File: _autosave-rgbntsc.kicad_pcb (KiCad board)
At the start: 2 copper layers, 50 x 70 mm, 40 parts, among them J1 USB_C_Receptacle_Power, J2 VGA, J3 SCART_CONN, J4 Mini-DIN-4, U1 LM1881, U102 74AHCT1G86, U103 74AHCT1G86, U2 SC6206B-65K5, U3 CXA2075, X1 ASE-14.32MHz

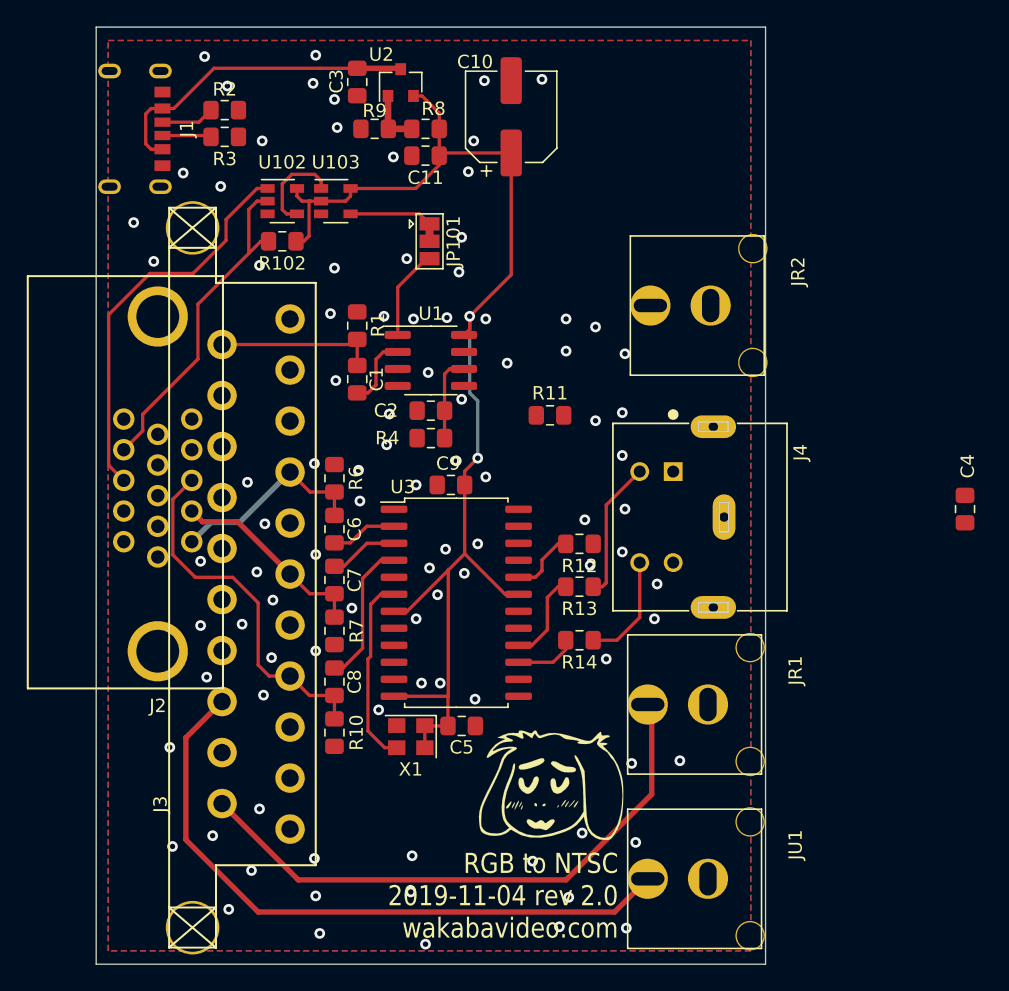
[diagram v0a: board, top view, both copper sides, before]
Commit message: CXA2075
Replaces AD724 with CXA2075, also adds GBS compatible RGB out header
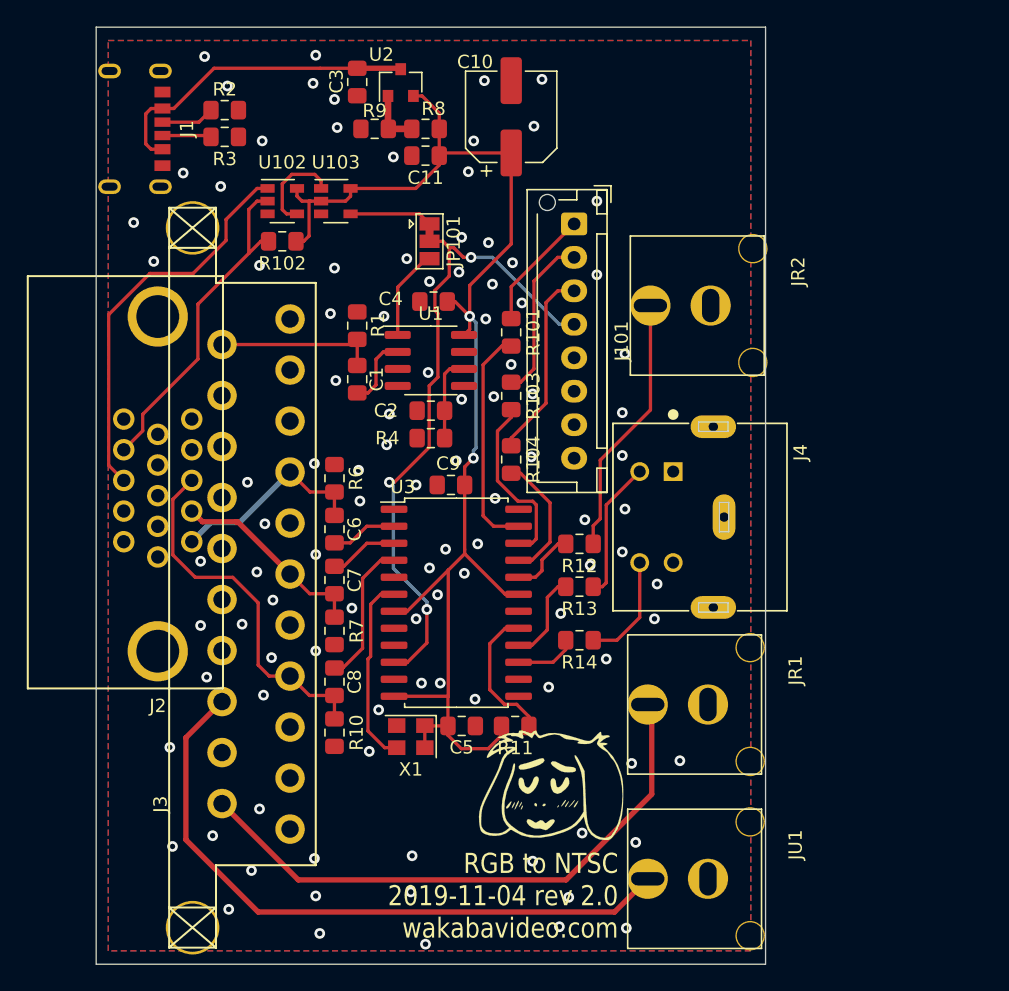
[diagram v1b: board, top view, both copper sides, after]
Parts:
- added J101: Conn_01x08, Connector_JST:JST_XH_B8B-XH-AM_1x08_P2.50mm_Vertical, F.Cu at (55.7, 54.7)
- added R101: 75, Resistor_SMD:R_0805_2012Metric_Pad1.15x1.40mm_HandSolder, F.Cu at (51.0, 62.8)
- added R103: 75, Resistor_SMD:R_0805_2012Metric_Pad1.15x1.40mm_HandSolder, F.Cu at (51.0, 67.5)
- added R104: 75, Resistor_SMD:R_0805_2012Metric_Pad1.15x1.40mm_HandSolder, F.Cu at (51.0, 72.3)
- moved C4 42.6 mm to (45.2, 60.5), turned to 180 degrees
- moved R11 23.3 mm to (51.3, 92.2), turned to 180 degrees
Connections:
- U3 pad 10: Net-(U3-Pad10) -> /SYNC
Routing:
- net /SYNC: track 0.00 -> 49.4 mm, vias 0 -> 3
- net Net-(JR2-Pad1): track 0.00 -> 19.6 mm
- net Net-(R101-Pad2): track 0.00 -> 16.9 mm
- net Net-(J101-Pad3): track 0.00 -> 14.2 mm
- net Net-(R103-Pad2): track 0.00 -> 13.4 mm
- net Net-(J101-Pad2): track 0.00 -> 12.4 mm
- net Net-(R11-Pad1): track 0.00 -> 10.5 mm
- net Net-(R104-Pad2): track 0.00 -> 9.67 mm
- net Net-(J101-Pad1): track 0.00 -> 9.02 mm
- net VCC: track 93.2 -> 101.5 mm
- net Net-(R104-Pad1): vias 0 -> 1
- net GND: vias 95 -> 102
